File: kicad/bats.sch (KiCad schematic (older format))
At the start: 28 parts, among them P1 SERVO, SW1 RESET, SW2 SHOT, SW3 UP, SW4 LEFT, SW5 DOWN, SW6 RIGHT, U1 BUZZER

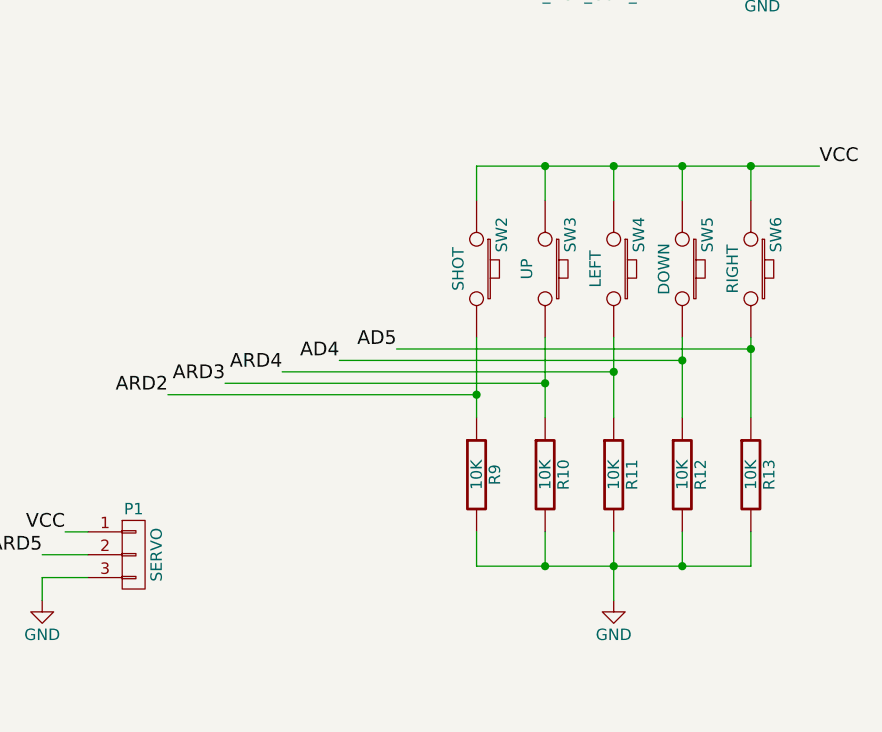
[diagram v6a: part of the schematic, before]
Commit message: Primeira versión con tres botóns. Ten pistas redundantes e hai que cambiar os pines dos botóns.
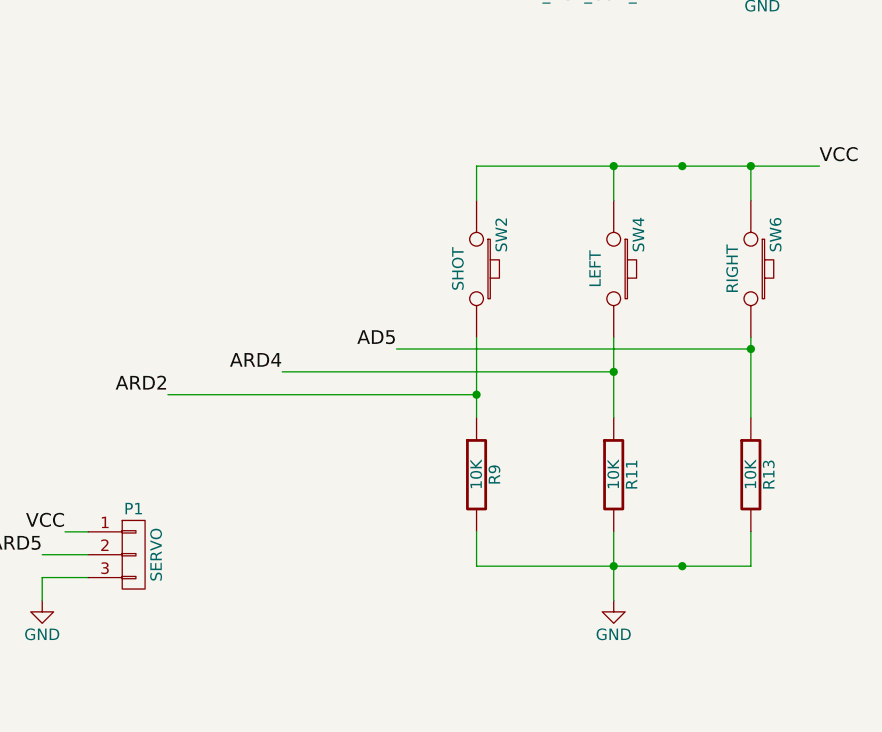
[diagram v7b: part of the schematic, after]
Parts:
- removed R10, R12: 10K, extra:Resistor_Horizontal_SmallHole_RM10mm, symbol R
- removed SW3: UP, FT:SW_PUSHBUTTON_PTH, symbol SW_PUSHBUTTON
- removed SW5: DOWN, FT:SW_PUSHBUTTON_PTH, symbol SW_PUSHBUTTON
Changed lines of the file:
@@
-$EndComp
-$Comp
-L R R10
-U 1 1 558AE59A
-P 9600 5200
-F 0 "R10" V 9680 5200 50  0000 C CNN
-F 1 "10K" V 9600 5200 50  0000 C CNN
-F 2 "extra:Resistor_Horizontal_SmallHole_RM10mm" H 9600 5200 60  0001 C CNN
-F 3 "" H 9600 5200 60  0000 C CNN
-	1    9600 5200
-	1    0    0    -1
 $EndComp
 $Comp
@@
 F 3 "" H 9900 5200 60  0000 C CNN
 	1    9900 5200
-	1    0    0    -1
-$EndComp
-$Comp
-L SW_PUSHBUTTON SW5
-U 1 1 558AEBB0
-P 10200 4300
-F 0 "SW5" H 10050 4410 50  0000 C CNN
-F 1 "DOWN" H 10200 4220 50  0000 C CNN
-F 2 "FT:SW_PUSHBUTTON_PTH" H 10200 4300 60  0001 C CNN
-F 3 "" H 10200 4300 60  0000 C CNN
-	1    10200 4300
-	0    1    1    0
-$EndComp
-$Comp
-L R R12
-U 1 1 558AEBB6
-P 10200 5200
-F 0 "R12" V 10280 5200 50  0000 C CNN
-F 1 "10K" V 10200 5200 50  0000 C CNN
-F 2 "extra:Resistor_Horizontal_SmallHole_RM10mm" H 10200 5200 60  0001 C CNN
-F 3 "" H 10200 5200 60  0000 C CNN
-	1    10200 5200
 	1    0    0    -1
 $EndComp
@@
 	6400 1150 6400 1450
 Wire Wire Line
-	9600 4600 9600 4950
-Wire Wire Line
 	9900 4600 9900 4950
 Wire Wire Line
-	10200 4600 10200 4950
-Wire Wire Line
 	10500 4600 10500 4950
 Wire Wire Line
 	9900 3850 9900 4000
-Wire Wire Line
-	10200 3850 10200 4000
 Connection ~ 9900 3850
 Wire Wire Line
@@
 	9300 3850 10800 3850
 Wire Wire Line
-	9600 3850 9600 4000
-Wire Wire Line
-	9600 5450 9600 5600
-Wire Wire Line
 	9300 5600 10500 5600
 Wire Wire Line
@@
 	9900 5450 9900 5750
 Connection ~ 9900 5600
-Wire Wire Line
-	10200 5450 10200 5600
 Connection ~ 10200 5600
 Wire Wire Line
@@
 Wire Wire Line
 	9300 4000 9300 3850
-Connection ~ 9600 3850
 Wire Wire Line
 	9300 5450 9300 5600
-Connection ~ 9600 5600
 Text Label 6750 4650 0    60   ~ 0
 ARD2
@@
 Text Label 8950 4650 2    60   ~ 0
 AD5
-Connection ~ 10200 4700
-Wire Wire Line
-	10200 4700 8700 4700
-Text Label 8700 4700 2    60   ~ 0
-AD4
 Connection ~ 9900 4750
 Wire Wire Line
@@
 Text Label 8450 4750 2    60   ~ 0
 ARD4
-Connection ~ 9600 4800
-Wire Wire Line
-	9600 4800 8200 4800
-Text Label 8200 4800 2    60   ~ 0
-ARD3
 Connection ~ 9300 4850
 Wire Wire Line
@@
 Text Label 7950 4850 2    60   ~ 0
 ARD2
-$Comp
-L SW_PUSHBUTTON SW3
-U 1 1 5589867E
-P 9600 4300
-F 0 "SW3" H 9450 4410 50  0000 C CNN
-F 1 "UP" H 9600 4220 50  0000 C CNN
-F 2 "FT:SW_PUSHBUTTON_PTH" H 9600 4300 60  0001 C CNN
-F 3 "" H 9600 4300 60  0000 C CNN
-	1    9600 4300
-	0    1    1    0
-$EndComp
 Text Label 4850 3850 2    60   ~ 0
 VCC

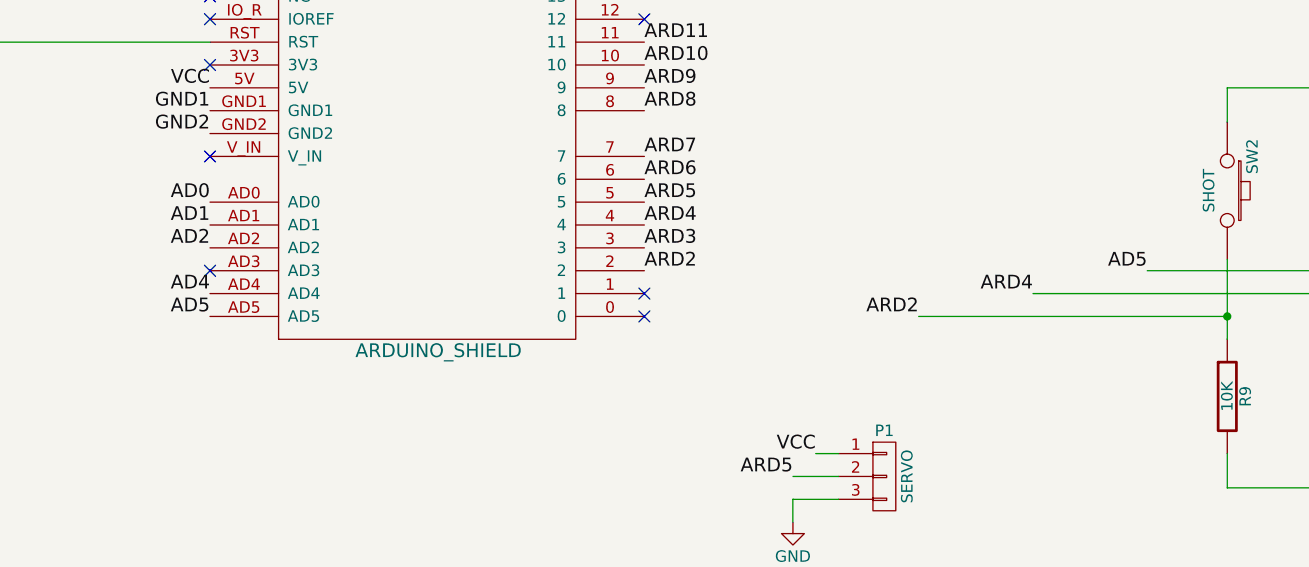
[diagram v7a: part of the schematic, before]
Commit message: Amañados os terminais dos botóns Compre rotar os botóns para simplificar as pistas
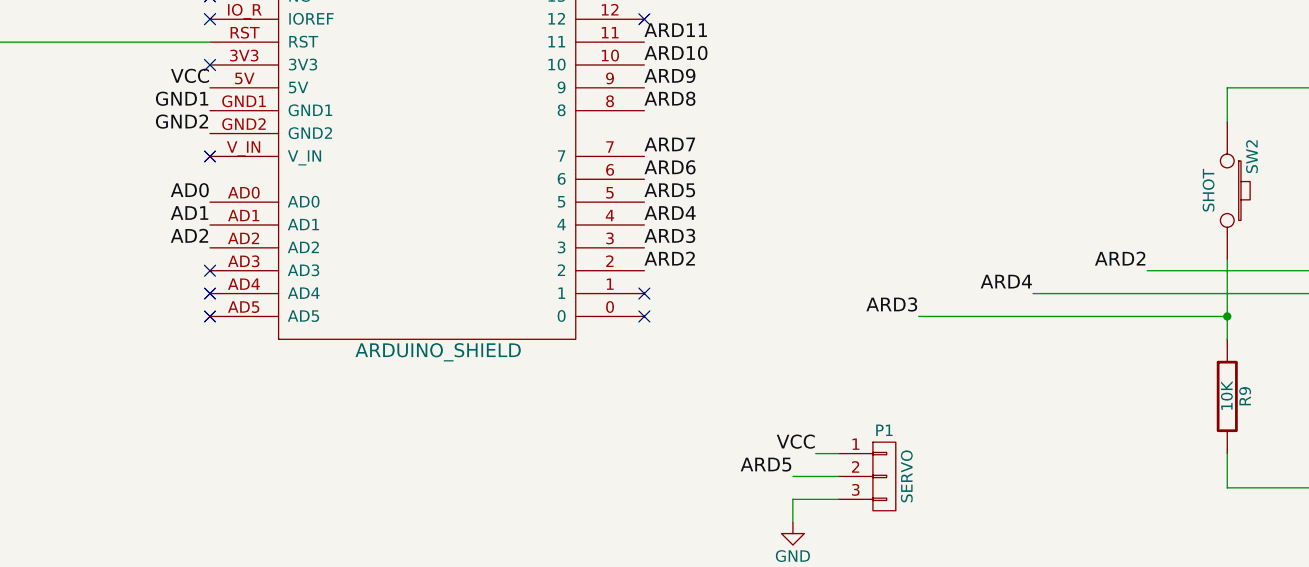
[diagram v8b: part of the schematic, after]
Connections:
- net ARD2: now also R13.1, SW6.2; no longer R9.1, SW2.2
- net ARD3: now also R9.1, SW2.2
- net AD4: no longer names the net of SHIELD1.AD4
- removed net AD5: R13.1, SHIELD1.AD5, SW6.2
- no-connect marks 17 -> 19
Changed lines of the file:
@@
 ARD8
 NoConn ~ 6750 3550
-Text Label 6750 4350 0    60   ~ 0
-ARD5
 Text Label 7400 5550 2    60   ~ 0
 ARD5
@@
 	10500 4650 8950 4650
 Text Label 8950 4650 2    60   ~ 0
-AD5
+ARD2
 Connection ~ 9900 4750
 Wire Wire Line
@@
 	9300 4850 7950 4850
 Text Label 7950 4850 2    60   ~ 0
-ARD2
+ARD3
 Text Label 4850 3850 2    60   ~ 0
 VCC
 NoConn ~ 6750 4750
 NoConn ~ 6750 4850
-Text Label 4850 4750 2    60   ~ 0
-AD4
-Text Label 4850 4850 2    60   ~ 0
-AD5
 Wire Wire Line
 	1925 3850 2650 3850
@@
 Text Label 4850 4550 2    60   ~ 0
 AD2
+NoConn ~ 4850 4750
+NoConn ~ 4850 4850
+Text Label 6750 4350 0    60   ~ 0
+ARD5
 $EndSCHEMATC
